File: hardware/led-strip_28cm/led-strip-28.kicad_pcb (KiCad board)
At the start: 2 copper layers, 280 x 10 mm, 49 parts, among them J1 Conn_01x01_Pin, J2 Conn_01x01_Pin, J3 Conn_01x01_Pin, J4 Conn_01x01_Pin, J5 Conn_01x01_Pin, J6 Conn_01x01_Pin, U1 LM317_TO-252

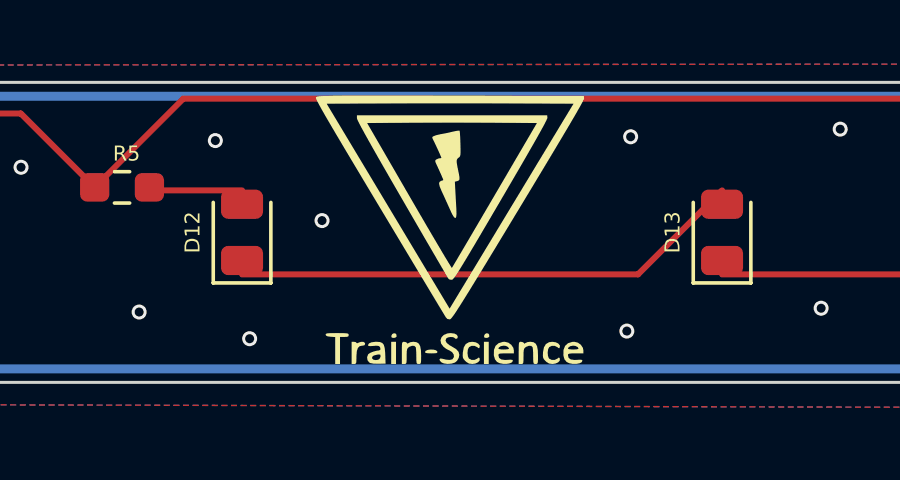
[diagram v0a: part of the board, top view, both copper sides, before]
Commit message: added manual to the repo
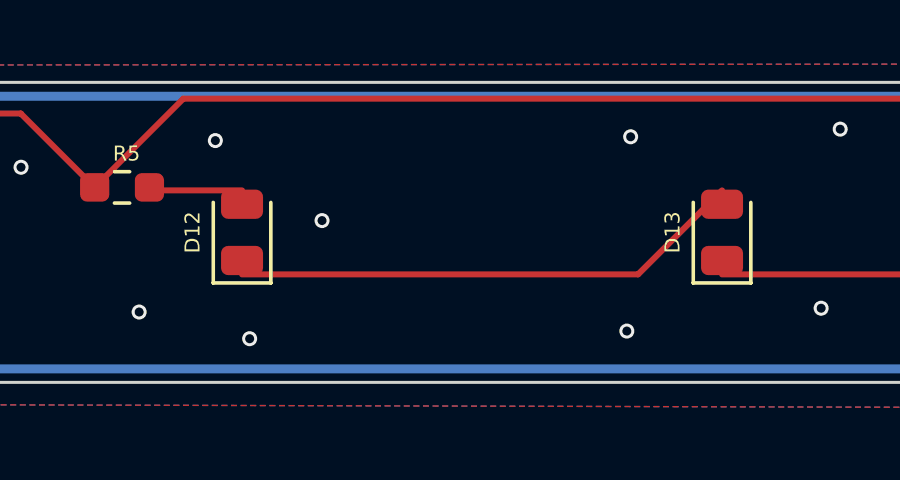
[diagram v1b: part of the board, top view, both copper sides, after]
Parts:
- removed G***: LOGO, custom_kicad_lib_sk:Train-Science logo small
